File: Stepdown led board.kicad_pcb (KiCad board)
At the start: 2 copper layers, 58.4 x 12.7 mm, 5 parts, among them J1 IN, J2 OUT, J3 Stepdown module

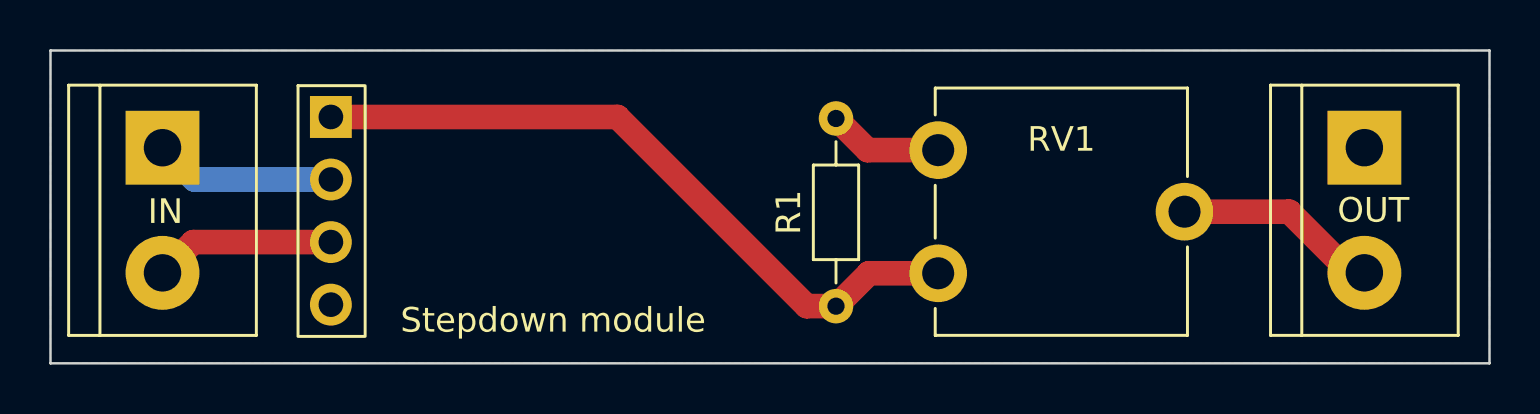
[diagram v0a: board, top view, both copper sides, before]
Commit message: - v1.1 (shorter version with component on both sides (WIP) - Reorganized production files folders
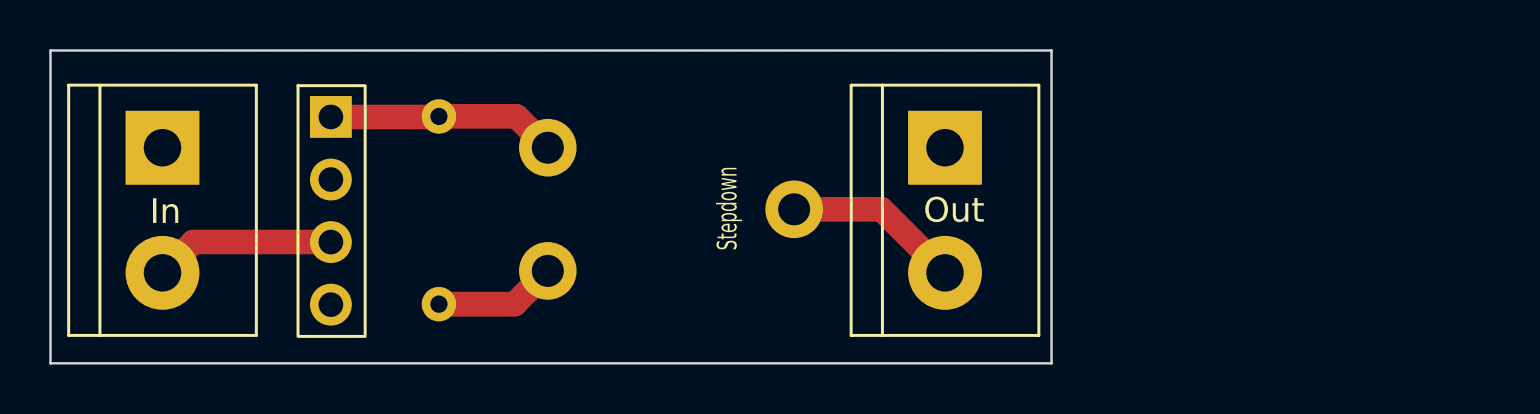
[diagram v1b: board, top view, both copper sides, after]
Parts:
- J1: value IN -> In
- J2: value OUT -> Out
- J3: value Stepdown module -> Stepdown
- R1, RV1: moved to B.Cu
- moved R1 17.9 mm to (36.1, 25.5), turned to -90 degrees
- moved J2 17.0 mm to (56.6, 26.8)
- moved RV1 16.6 mm to (40.5, 26.8)
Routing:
- net Vout: track 28.4 -> 9.34 mm
- net GND: track 7.37 -> 0.00 mm
- net Vled: track 7.76 -> 7.19 mm
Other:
- board size 58.4 x 12.7 mm -> 40.6 x 12.7 mm
- board text added: "v1.1"
- board text removed: "v1.0"

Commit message: Version 1.1.0 WIP
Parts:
- J1: value In -> IN
- J2: value Out -> OUT
- R1: footprint Resistor_THT:R_Axial_DIN0204_L3.6mm_D1.6mm_P7.62mm_Horizontal -> Resistor_SMD:R_2816_7142Metric_Pad3.20x4.45mm_HandSolder
- RV1: footprint Potentiometer_THT:Potentiometer_ACP_CA9-V10_Vertical -> Potentiometer_SMD:Potentiometer_ACP_CA6-VSMD_Vertical
- moved R1 11.8 mm to (47.3, 29.2), turned to 180 degrees
- moved J1 5.15 mm to (24.5, 32.0), turned to 90 degrees
- moved RV1 3.40 mm to (38.1, 29.2), turned to -90 degrees
- moved J2 2.49 mm to (54.1, 26.9)
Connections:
- J2 pad 1: GND -> Net-(J2-Pad1)
- J3 pad 1: Vout -> unconnected-(J3-Pad1)
- J3 pad 2: GND -> +12V
- J3 pad 3: +12V -> GND
- J3 pad 4: unconnected-(J3-Pad4) -> Vout
- R1 pad 1: Vout -> Net-(J2-Pad1)
- R1 pad 2: Net-(R1-Pad2) -> GND
- RV1 pad 1: Vout -> GND
- RV1 pad 3: Net-(R1-Pad2) -> Vout
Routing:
- net Vled: track 7.19 -> 16.7 mm
- net Net-(J2-Pad1): track 0.00 -> 5.21 mm
- net Net-(R1-Pad2): track 4.98 -> 0.00 mm
- net Vout: track 9.34 -> 10.9 mm
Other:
- board size 40.6 x 12.7 mm -> 38.1 x 12.7 mm
- board text added: "v1.1.0"
- board text removed: "v1.1"

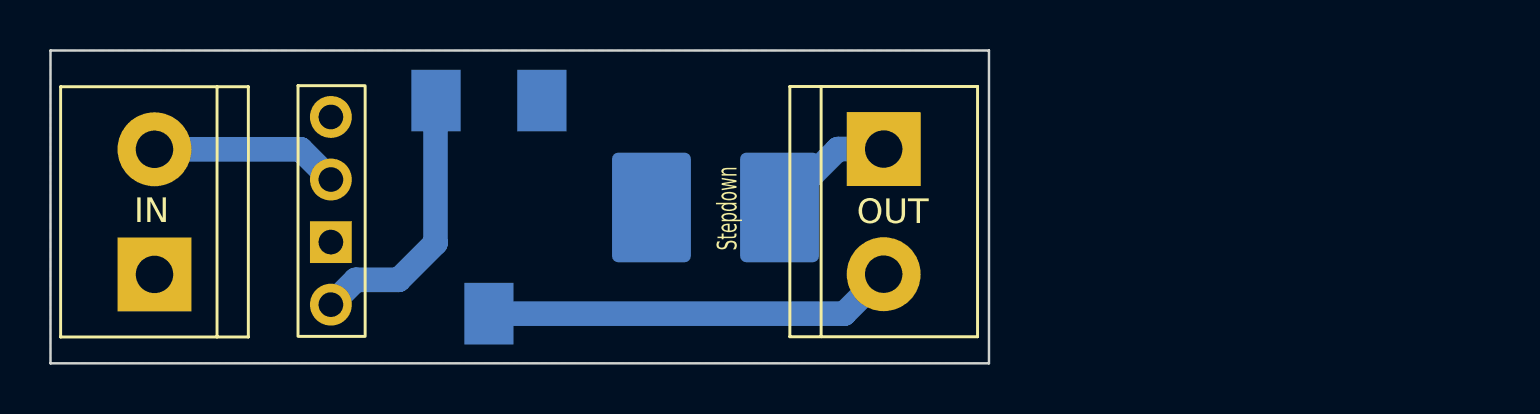
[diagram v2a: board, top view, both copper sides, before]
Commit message: - Schematic cleanup - Layout (silk) update
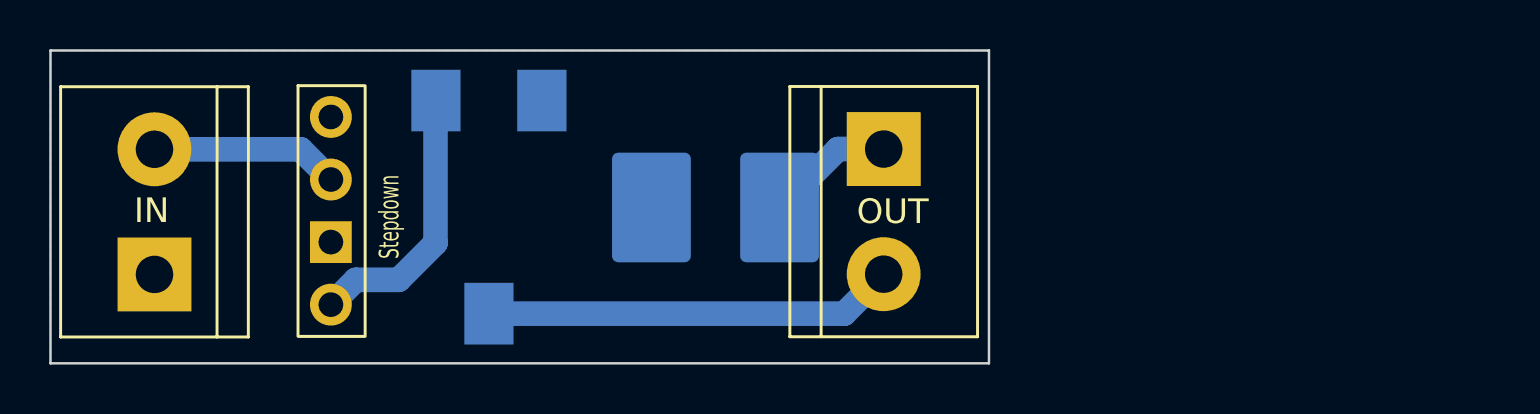
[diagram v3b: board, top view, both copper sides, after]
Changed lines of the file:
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@@
       (effects (font (size 1 1) (thickness 0.15)))
     )
-    (fp_text value "Stepdown" (at 16.095787 3.713746 90) (layer "F.SilkS")
+    (fp_text value "Stepdown" (at 2.372547 4.054615 90) (layer "F.SilkS")
       (effects (font (size 0.8 0.5) (thickness 0.125)))
     )
@@
   (segment (start 52.288759 26.861402) (end 54.145624 26.861402) (width 1) (layer "B.Cu") (net 5))
   (zone (net 1) (net_name "GND") (layer "B.Cu") (hatch edge 0.508)
-    (connect_pads (clearance 0.508))
+    (connect_pads (clearance 0.3))
     (min_thickness 0.254) (filled_areas_thickness no)
     (fill yes (thermal_gap 0.508) (thermal_bridge_width 0.508))
